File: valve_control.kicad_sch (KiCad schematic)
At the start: 0 parts

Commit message: Add ESP32-S3-WROOM-1, 5V rail and UI sheet
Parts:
- added U4: ULN2003V12, symbol Transistor_Array:ULN2003
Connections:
- new net +15V: U4.9 (COM)
- new net GND: U4.8 (GND)
- new net VALVE1_CTRL: U4.1 (I1)
- new net VALVE1_GND: U4.16 (O1)
- new net VALVE2_CTRL: U4.2 (I2), U4.7 (I7)
- new net VALVE2_GND: U4.10 (O7), U4.15 (O2)
- new net VALVE3_CTRL: U4.3 (I3)
- new net VALVE3_GND: U4.14 (O3)
- new net VALVE4_CTRL: U4.4 (I4)
- new net VALVE4_GND: U4.13 (O4)
- new net VALVE5_CTRL: U4.5 (I5)
- new net VALVE5_GND: U4.12 (O5)
- new net VALVE6_CTRL: U4.6 (I6)
- new net VALVE6_GND: U4.11 (O6)
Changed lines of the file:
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@@
     (rev "1.0")
   )
+  (wire (pts (xy 123.19 96.52) (xy 130.81 96.52))
+    (stroke (width 0) (type default))
+  )
+  (wire (pts (xy 151.13 93.98) (xy 157.48 93.98))
+    (stroke (width 0) (type default))
+  )
+  (wire (pts (xy 123.19 88.9) (xy 130.81 88.9))
+    (stroke (width 0) (type default))
+  )
+  (wire (pts (xy 123.19 104.14) (xy 130.81 104.14))
+    (stroke (width 0) (type default))
+  )
+  (wire (pts (xy 151.13 96.52) (xy 157.48 96.52))
+    (stroke (width 0) (type default))
+  )
+  (wire (pts (xy 140.97 109.22) (xy 140.97 111.76))
+    (stroke (width 0) (type default))
+  )
+  (wire (pts (xy 123.19 91.44) (xy 130.81 91.44))
+    (stroke (width 0) (type default))
+  )
+  (wire (pts (xy 151.13 99.06) (xy 157.48 99.06))
+    (stroke (width 0) (type default))
+  )
+  (wire (pts (xy 151.13 88.9) (xy 157.48 88.9))
+    (stroke (width 0) (type default))
+  )
+  (wire (pts (xy 123.19 99.06) (xy 130.81 99.06))
+    (stroke (width 0) (type default))
+  )
+  (wire (pts (xy 157.48 83.82) (xy 157.48 73.66))
+    (stroke (width 0) (type default))
+  )
+  (wire (pts (xy 151.13 83.82) (xy 157.48 83.82))
+    (stroke (width 0) (type default))
+  )
+  (wire (pts (xy 151.13 91.44) (xy 157.48 91.44))
+    (stroke (width 0) (type default))
+  )
+  (wire (pts (xy 123.19 101.6) (xy 130.81 101.6))
+    (stroke (width 0) (type default))
+  )
+  (wire (pts (xy 151.13 101.6) (xy 157.48 101.6))
+    (stroke (width 0) (type default))
+  )
+  (wire (pts (xy 151.13 104.14) (xy 157.48 104.14))
+    (stroke (width 0) (type default))
+  )
+  (wire (pts (xy 123.19 93.98) (xy 130.81 93.98))
+    (stroke (width 0) (type default))
+  )
+  (hierarchical_label "VALVE6_CTRL" (shape input) (at 123.19 101.6 180) (fields_autoplaced)
+    (effects (font (size 1.27 1.27)) (justify right))
+  )
+  (hierarchical_label "VALVE1_GND" (shape input) (at 157.48 88.9 0) (fields_autoplaced)
+    (effects (font (size 1.27 1.27)) (justify left))
+  )
+  (hierarchical_label "VALVE3_GND" (shape input) (at 157.48 93.98 0) (fields_autoplaced)
+    (effects (font (size 1.27 1.27)) (justify left))
+  )
+  (hierarchical_label "VALVE2_CTRL" (shape input) (at 123.19 104.14 180) (fields_autoplaced)
+    (effects (font (size 1.27 1.27)) (justify right))
+  )
+  (hierarchical_label "VALVE5_GND" (shape input) (at 157.48 99.06 0) (fields_autoplaced)
+    (effects (font (size 1.27 1.27)) (justify left))
+  )
+  (hierarchical_label "VALVE6_GND" (shape input) (at 157.48 101.6 0) (fields_autoplaced)
+    (effects (font (size 1.27 1.27)) (justify left))
+  )
+  (hierarchical_label "VALVE2_GND" (shape input) (at 157.48 91.44 0) (fields_autoplaced)
+    (effects (font (size 1.27 1.27)) (justify left))
+  )
+  (hierarchical_label "VALVE4_GND" (shape input) (at 157.48 96.52 0) (fields_autoplaced)
+    (effects (font (size 1.27 1.27)) (justify left))
+  )
+  (hierarchical_label "VALVE2_GND" (shape input) (at 157.48 104.14 0) (fields_autoplaced)
+    (effects (font (size 1.27 1.27)) (justify left))
+  )
+  (hierarchical_label "VALVE1_CTRL" (shape input) (at 123.19 88.9 180) (fields_autoplaced)
+    (effects (font (size 1.27 1.27)) (justify right))
+  )
+  (hierarchical_label "VALVE3_CTRL" (shape input) (at 123.19 93.98 180) (fields_autoplaced)
+    (effects (font (size 1.27 1.27)) (justify right))
+  )
+  (hierarchical_label "VALVE4_CTRL" (shape input) (at 123.19 96.52 180) (fields_autoplaced)
+    (effects (font (size 1.27 1.27)) (justify right))
+  )
+  (hierarchical_label "VALVE2_CTRL" (shape input) (at 123.19 91.44 180) (fields_autoplaced)
+    (effects (font (size 1.27 1.27)) (justify right))
+  )
+  (hierarchical_label "VALVE5_CTRL" (shape input) (at 123.19 99.06 180) (fields_autoplaced)
+    (effects (font (size 1.27 1.27)) (justify right))
+  )
+  (symbol (lib_id "Transistor_Array:ULN2003") (at 140.97 93.98 0) (unit 1)
+    (in_bom yes) (on_board yes) (dnp no) (fields_autoplaced)
+    (property "Reference" "U4" (at 140.97 76.2 0)
+      (effects (font (size 1.27 1.27)))
+    )
+    (property "Value" "ULN2003V12" (at 140.97 78.74 0)
+      (effects (font (size 1.27 1.27)))
+    )
+    (property "Footprint" "" (at 142.24 107.95 0)
+      (effects (font (size 1.27 1.27)) (justify left) hide)
+    )
+    (property "Datasheet" "https://www.ti.com/lit/ds/symlink/uln2003v12.pdf" (at 143.51 99.06 0)
+      (effects (font (size 1.27 1.27)) hide)
+    )
+    (pin "2")
+    (pin "10")
+    (pin "8")
+    (pin "13")
+    (pin "11")
+    (pin "12")
+    (pin "3")
+    (pin "15")
+    (pin "14")
+    (pin "6")
+    (pin "9")
+    (pin "1")
+    (pin "5")
+    (pin "4")
+    (pin "16")
+    (pin "7")
+    (instances
+      (project "mainboard"
+        (path "/613f8c39-c37c-4981-8911-5138d36a7959/e9806059-9dec-41fc-a77f-d545160fc79f"
+          (reference "U4") (unit 1)
+        )
+      )
+    )
+  )
+  (symbol (lib_id "power:GND") (at 140.97 111.76 0) (unit 1)
+    (in_bom yes) (on_board yes) (dnp no) (fields_autoplaced)
+    (property "Reference" "#PWR024" (at 140.97 118.11 0)
+      (effects (font (size 1.27 1.27)) hide)
+    )
+    (property "Value" "GND" (at 140.97 116.84 0)
+      (effects (font (size 1.27 1.27)))
+    )
+    (property "Footprint" "" (at 140.97 111.76 0)
+      (effects (font (size 1.27 1.27)) hide)
+    )
+    (property "Datasheet" "" (at 140.97 111.76 0)
+      (effects (font (size 1.27 1.27)) hide)
+    )
+    (pin "1")
+    (instances
+      (project "mainboard"
+        (path "/613f8c39-c37c-4981-8911-5138d36a7959/e9806059-9dec-41fc-a77f-d545160fc79f"
+          (reference "#PWR024") (unit 1)
+        )
+      )
+    )
+  )
+  (symbol (lib_id "power:+15V") (at 157.48 73.66 0) (unit 1)
+    (in_bom yes) (on_board yes) (dnp no) (fields_autoplaced)
+    (property "Reference" "#PWR023" (at 157.48 77.47 0)
+      (effects (font (size 1.27 1.27)) hide)
+    )
+    (property "Value" "+15V" (at 157.48 68.58 0)
+      (effects (font (size 1.27 1.27)))
+    )
+    (property "Footprint" "" (at 157.48 73.66 0)
+      (effects (font (size 1.27 1.27)) hide)
+    )
+    (property "Datasheet" "" (at 157.48 73.66 0)
+      (effects (font (size 1.27 1.27)) hide)
+    )
+    (pin "1")
+    (instances
+      (project "mainboard"
+        (path "/613f8c39-c37c-4981-8911-5138d36a7959/e9806059-9dec-41fc-a77f-d545160fc79f"
+          (reference "#PWR023") (unit 1)
+        )
+      )
+    )
+  )
 )

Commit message: Finish first design
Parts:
- removed U4: ULN2003V12, symbol Transistor_Array:ULN2003
- added D10, D4, D5, D6, D7, D8, D9: S1A-13-F, Diode_SMD:D_SMA, symbol Device:D
- added Q10, Q4, Q5, Q6, Q7, Q8, Q9: IRLML2502, Package_TO_SOT_SMD:SOT-23, symbol Device:Q_NMOS_GSD
- added R11, R18, R20, R22, R24, R26, R28: R100k, Resistor_SMD:R_0805_2012Metric, symbol Device:R
- added R16, R17, R19, R21, R23, R25, R27: R120, Resistor_SMD:R_0805_2012Metric, symbol Device:R
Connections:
- net +15V: now also D10.1 (K), D4.1 (K), D5.1 (K), D6.1 (K), D7.1 (K), D8.1 (K), D9.1 (K)
- net GND: now also Q10.2 (S), Q4.2 (S), Q5.2 (S), Q6.2 (S), Q7.2 (S), Q8.2 (S), Q9.2 (S), R11.1, R18.1, R20.1, R22.1, R24.1, R26.1, R28.1
- net VALVE1_CTRL: now also R17.1
- net VALVE1_GND: now also D4.2 (A), Q4.3 (D)
- net VALVE2_CTRL: now also R16.1
- net VALVE2_GND: now also D5.2 (A), Q5.3 (D)
- net VALVE3_CTRL: now also R19.1
- net VALVE3_GND: now also D6.2 (A), Q6.3 (D)
- net VALVE4_CTRL: now also R21.1
- net VALVE4_GND: now also D7.2 (A), Q7.3 (D)
- net VALVE5_CTRL: now also R23.1
- net VALVE5_GND: now also D8.2 (A), Q8.3 (D)
- net VALVE6_CTRL: now also R25.1
- net VALVE6_GND: now also D9.2 (A), Q9.3 (D)
- new net VALVE1_GATE: Q4.1 (G), R11.2, R17.2
- new net VALVE2_GATE: Q5.1 (G), R16.2, R18.2
- new net VALVE3_GATE: Q6.1 (G), R19.2, R20.2
- new net VALVE4_GATE: Q7.1 (G), R21.2, R22.2
- new net VALVE5_GATE: Q8.1 (G), R23.2, R24.2
- new net VALVE6_GATE: Q9.1 (G), R25.2, R26.2
- new net VALVE7_GATE: Q10.1 (G), R27.2, R28.2
- new net VALVE7_GND: D10.2 (A), Q10.3 (D)
- new net VAVLE7_CTRL: R27.1

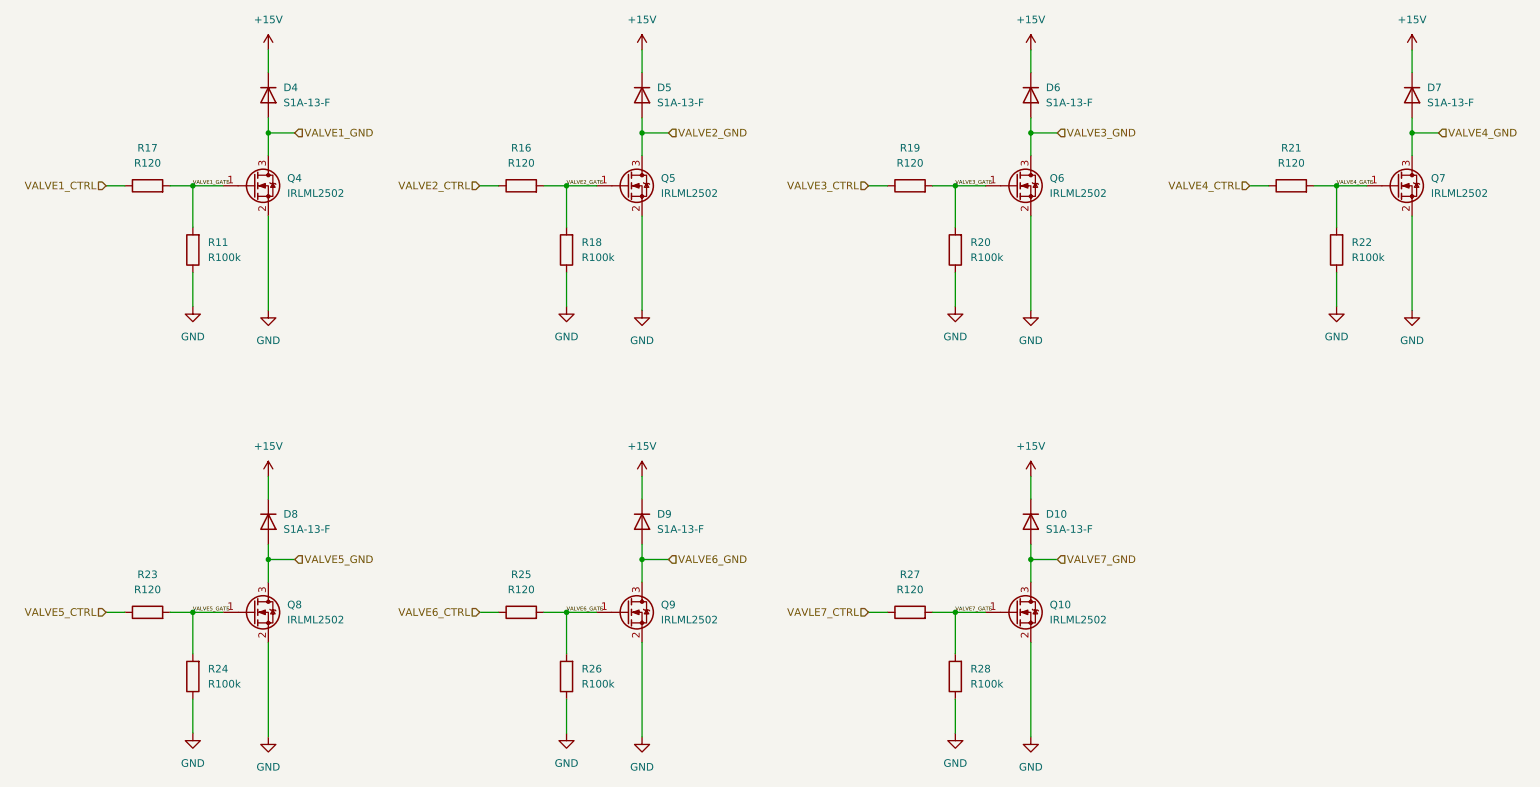
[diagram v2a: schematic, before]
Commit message: Re-annotate parts by board
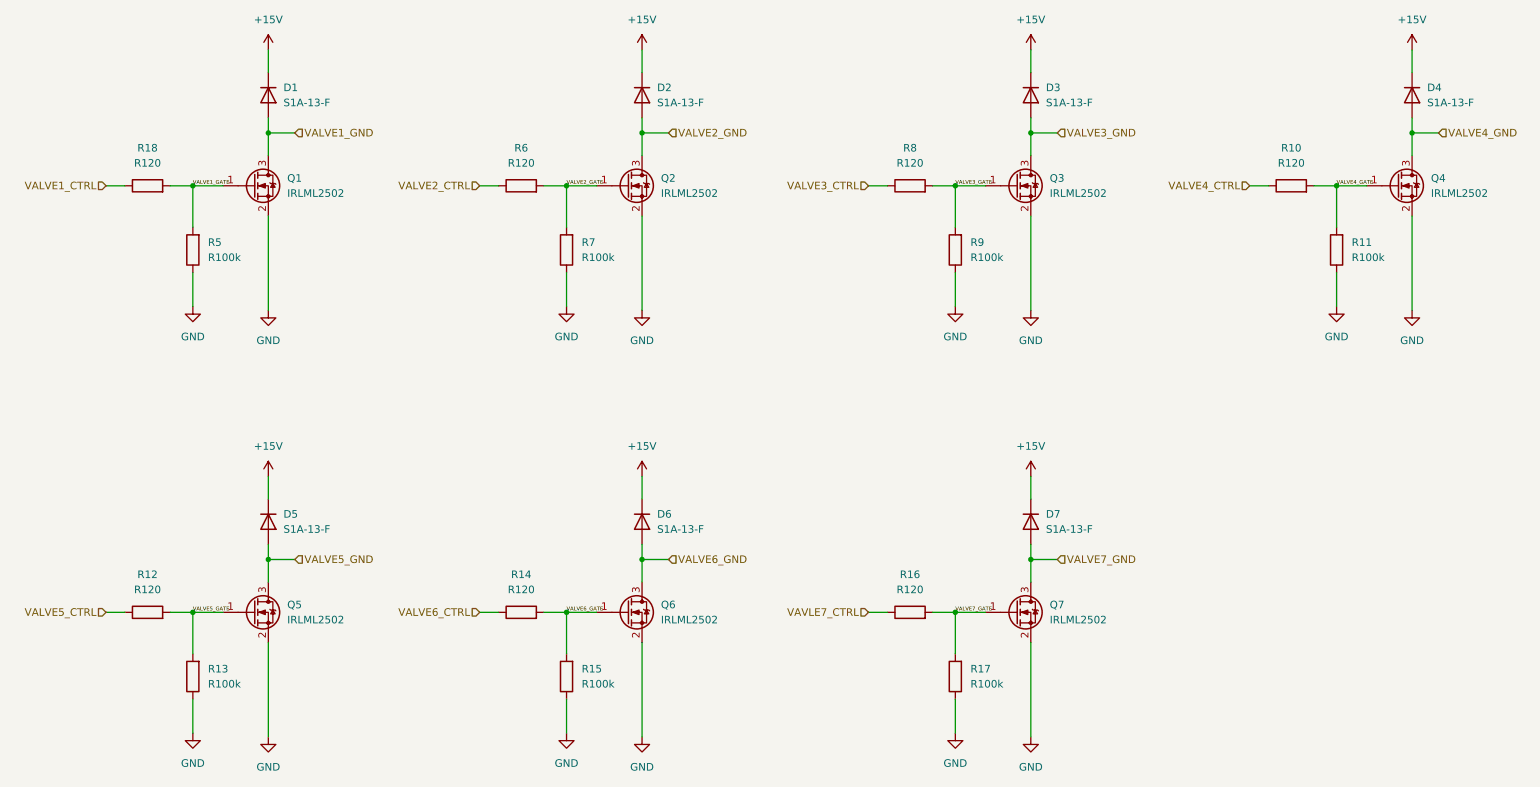
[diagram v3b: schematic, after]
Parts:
- renumbered D4 to D1, D5 to D2, D6 to D3, D7 to D4, D8 to D5, D9 to D6, D10 to D7, Q4 to Q1, Q5 to Q2, Q6 to Q3, Q7 to Q4, Q8 to Q5, Q9 to Q6, Q10 to Q7, R21 to R10, R22 to R11, R23 to R12, R24 to R13, R25 to R14, R26 to R15, R27 to R16, R28 to R17, R17 to R18, R11 to R5, R16 to R6, R18 to R7, R19 to R8, R20 to R9

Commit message: Redesign power rails to use barrel jack 12V input
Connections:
- net +15V renamed +12V

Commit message: Reannotate geographically by layout
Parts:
- renumbered R11 to R10, R12 to R11, R13 to R12, R14 to R13, R15 to R14, R16 to R15, R17 to R16, R18 to R3, R5 to R4, R6 to R5, R7 to R6, R8 to R7, R9 to R8, R10 to R9

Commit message: Fix revision
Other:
- title: openautolab - Mainboard -> openautolab - Alternative Mainboard
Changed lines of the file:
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@@
   (paper "A4")
   (title_block
-    (title "openautolab - Mainboard")
+    (title "openautolab - Alternative Mainboard")
     (date "2024-04-03")
-    (rev "2.0")
+    (rev "1")
   )
   (junction (at 60.325 111.125) (diameter 0) (color 0 0 0 0)
